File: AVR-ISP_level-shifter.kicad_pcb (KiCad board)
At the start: 2 copper layers, 0 parts

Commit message: Might be done!
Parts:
- added C1: 1µF, Resistors_SMD:R_0603, B.Cu at (63.2, 55.0)
- added C2: 1µF, Resistors_SMD:R_0603, B.Cu at (66.0, 53.2)
- added INPUT1: AVR-ISP-6, DIL-Headers:DIL-3, F.Cu at (50.0, 49.2)
- added INPUT2: AVR-ISP-10, DIL-Headers:DIL-5, F.Cu at (56.2, 49.2)
- added LOGO1: LED_smile_silkscreen_5mm, led-smile:LED_smile_silkscreen_5mm, B.Cu at (49.9, 56.1)
- added LOGO2: OSHW-logo_silkscreen_5mm, oshw-logo:OSHW-logo_silkscreen_5mm, B.Cu at (86.8, 56.1)
- added OUTPUT1: AVR-ISP-6, DIL-Headers:DIL-3, F.Cu at (86.5, 49.2)
- added OUTPUT2: AVR-ISP-10, DIL-Headers:DIL-5, F.Cu at (80.8, 49.2)
- added Q1: BSS138, Housings_SOT-23_SOT-143_TSOT-6:SOT-23, F.Cu at (63.0, 42.5)
- added Q2: BSS138, Housings_SOT-23_SOT-143_TSOT-6:SOT-23, F.Cu at (66.2, 42.5)
- added Q3: BSS138, Housings_SOT-23_SOT-143_TSOT-6:SOT-23, F.Cu at (63.0, 47.0)
- added Q4: BSS138, Housings_SOT-23_SOT-143_TSOT-6:SOT-23, F.Cu at (66.2, 47.0)
- added Q5: BSS138, Housings_SOT-23_SOT-143_TSOT-6:SOT-23, F.Cu at (63.0, 51.5)
- added Q6: BSS138, Housings_SOT-23_SOT-143_TSOT-6:SOT-23, F.Cu at (66.2, 51.5)
- added Q7: BSS138, Housings_SOT-23_SOT-143_TSOT-6:SOT-23, F.Cu at (63.0, 56.0)
- added Q8: BSS138, Housings_SOT-23_SOT-143_TSOT-6:SOT-23, F.Cu at (66.2, 56.0)
- added R1: 1K5, Resistors_SMD:R_0603, F.Cu at (60.5, 42.5)
- added R2: 1K5, Resistors_SMD:R_0603, F.Cu at (68.8, 42.5)
- added R3: 1K5, Resistors_SMD:R_0603, F.Cu at (60.5, 47.0)
- added R4: 1K5, Resistors_SMD:R_0603, F.Cu at (68.8, 47.0)
- added R5: 1K5, Resistors_SMD:R_0603, F.Cu at (60.5, 51.5)
- added R6: 1K5, Resistors_SMD:R_0603, F.Cu at (68.8, 51.5)
- added R7: 1K5, Resistors_SMD:R_0603, F.Cu at (60.5, 56.0)
- added R8: 1K5, Resistors_SMD:R_0603, F.Cu at (68.8, 56.0)
- added SW1: APEM 25439NH, Switches:switch_vert_SPDT_ON-OFF-ON_TH_APEM-25439NH, F.Cu at (73.8, 49.2)
- added U1: AMS1117-3.3, SMD_Packages:SOT-223, B.Cu at (64.8, 47.5)
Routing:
- net /GND: track 0.00 -> 113.4 mm
- net /VCC_PRG: track 0.00 -> 71.0 mm, vias 0 -> 4
- net /VCC_TARGET: track 0.00 -> 51.1 mm
- net /MISO_TARGET: track 0.00 -> 34.4 mm
- net /SCK_TARGET: track 0.00 -> 26.3 mm, vias 0 -> 2
- net /MOSI_TARGET: track 0.00 -> 25.8 mm, vias 0 -> 2
- net /RESET_TARGET: track 0.00 -> 24.4 mm, vias 0 -> 2
- net /MISO_PRG: track 0.00 -> 23.1 mm
- net /MOSI_PRG: track 0.00 -> 22.8 mm
- net /RESET_PRG: track 0.00 -> 20.8 mm
- net /VCC_REG: track 0.00 -> 16.4 mm
- net /SCK_PRG: track 0.00 -> 13.9 mm
- net Net-(Q7-Pad3): track 0.00 -> 1.25 mm
- net Net-(Q5-Pad3): track 0.00 -> 1.25 mm
- net Net-(Q3-Pad3): track 0.00 -> 1.25 mm
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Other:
- board outline added: 44 x 20 mm
- net class Default: trace_width 0.3048 -> 0.2032
- net class power added: clearance 0.2032, trace_width 0.4064, via_dia 0.635, via_drill 0.3302
- board text added: "2015 - blog.spitzenpfeil.org"
- board text added: "3.3V"
- board text added: "5V"
- board text added: "AVR-ISP"
- board text added: "AVR-ISP level-shifter 0.10.a"
- board text added: "INPUT"
- board text added: "OUTPUT"

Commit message: Tweaks.
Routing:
- net /MOSI_TARGET: track 25.8 -> 25.3 mm
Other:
- board text added: "[3.3-OFF-5]"

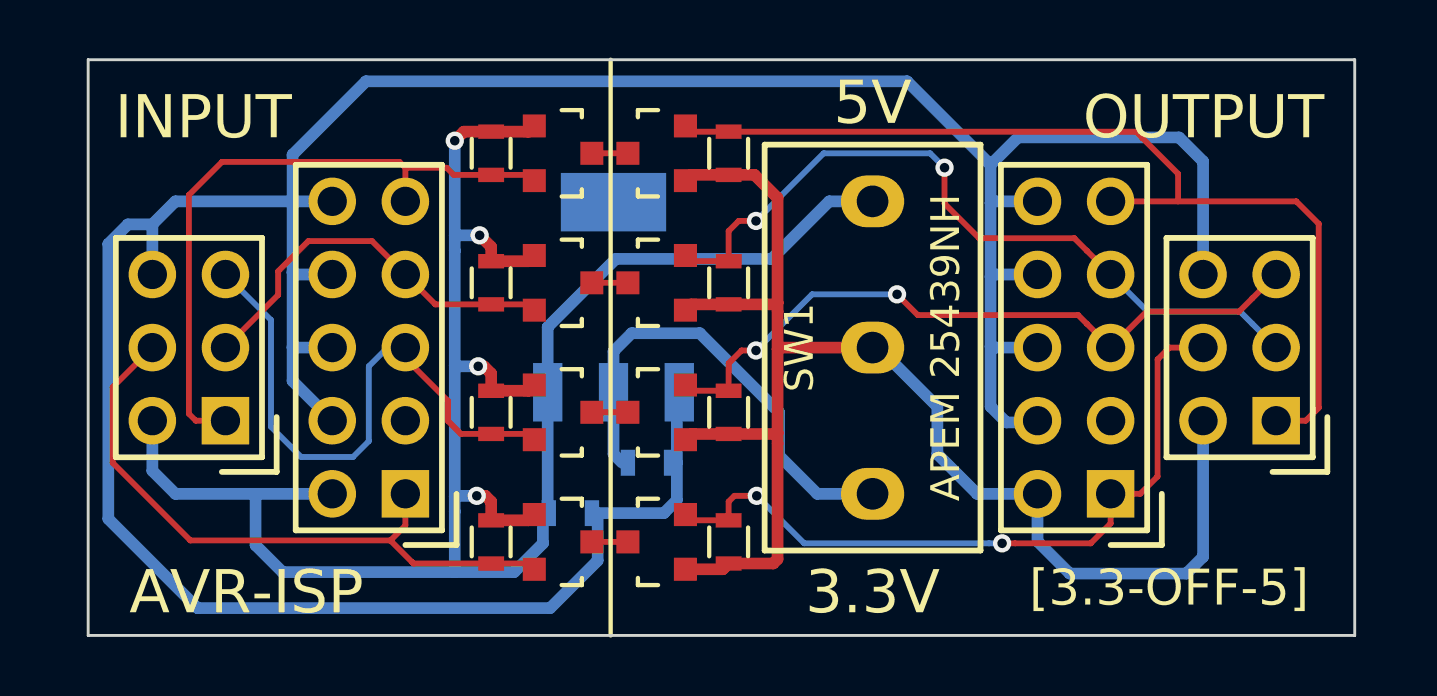
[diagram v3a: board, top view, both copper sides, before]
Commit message: Added shortened URL to github repo to board.
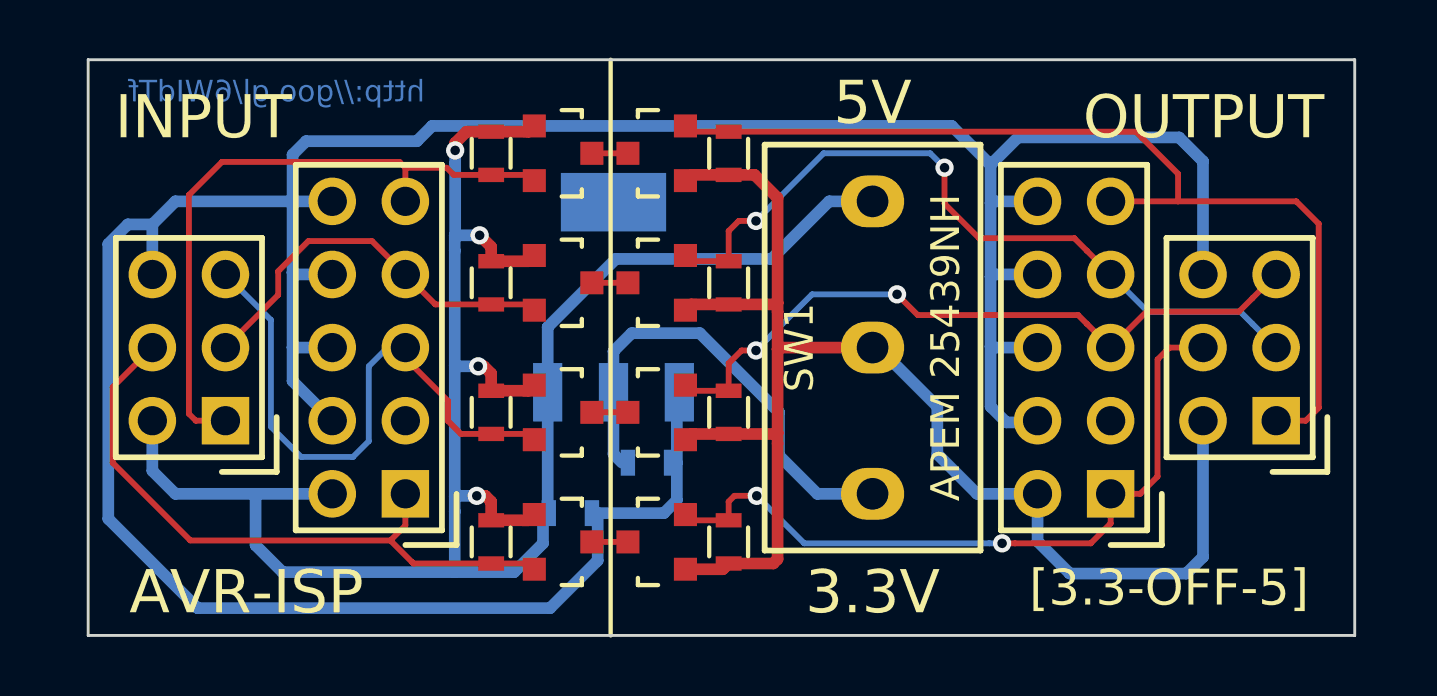
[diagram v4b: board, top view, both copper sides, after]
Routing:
- net /GND: track 113.4 -> 112.1 mm
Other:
- board text added: "http://goo.gl/6WIdTf"

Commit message: Added comment to schematic + silkscreen tweaks.
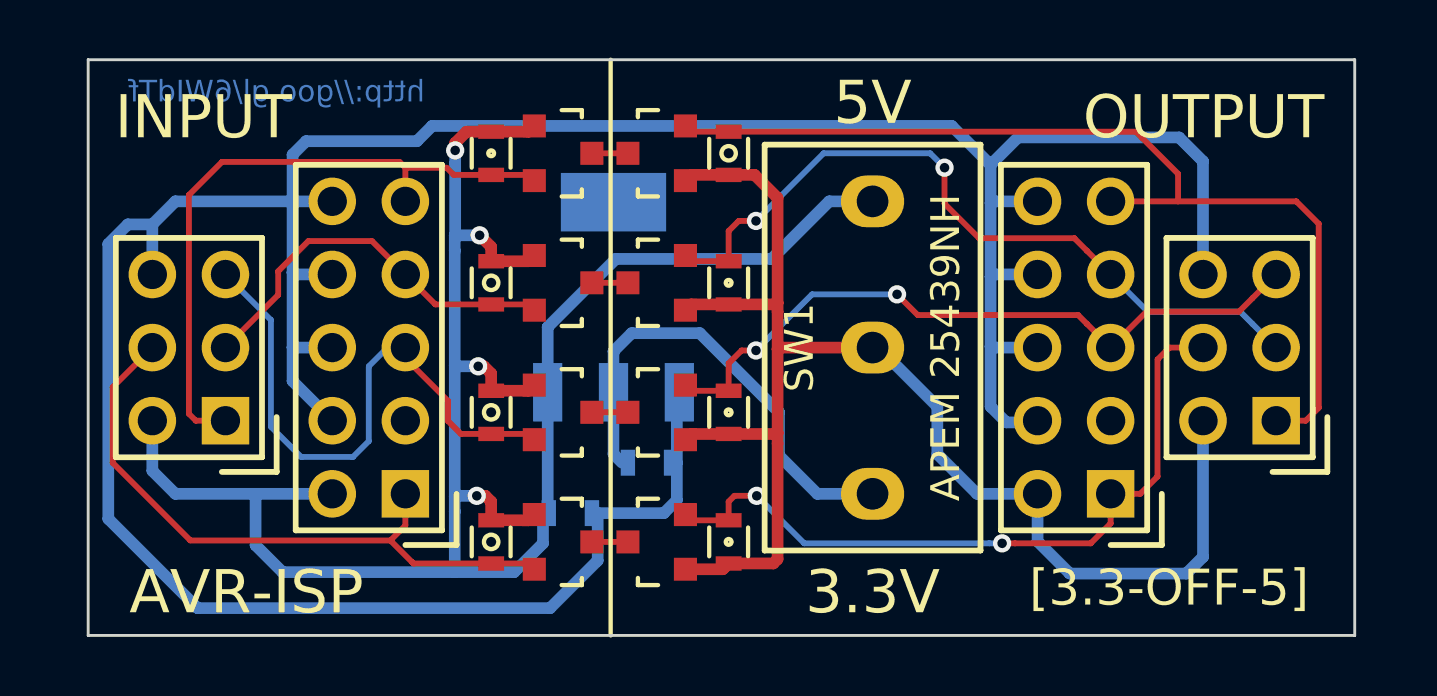
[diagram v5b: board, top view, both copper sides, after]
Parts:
- renumbered R2 to DR.R2, R3 to DR.R3, R5 to DR.R5, R7 to DR.R7
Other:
- board text added: "AVR-ISP level-shifter 0.11.a"
- board text removed: "AVR-ISP level-shifter 0.10.a"

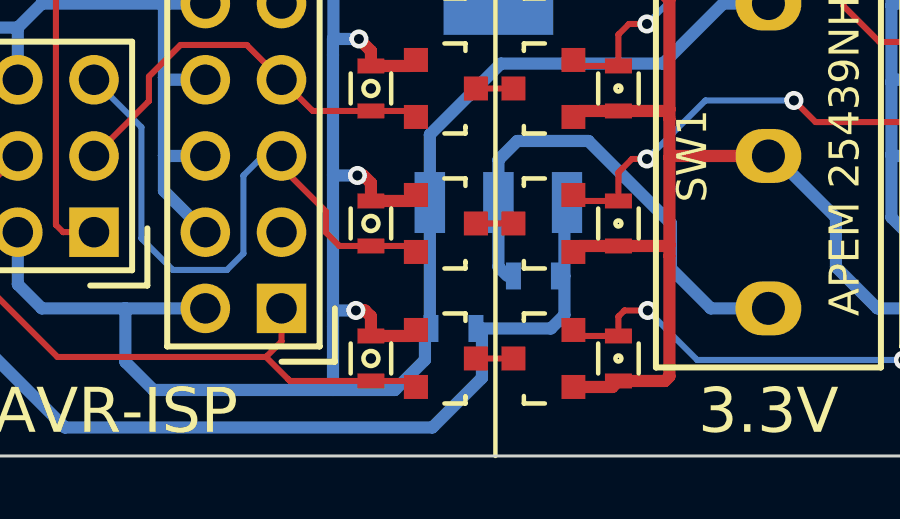
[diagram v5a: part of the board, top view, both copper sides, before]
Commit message: Added load resistor (~300R) to pull minimum load current out of 3.3V LDO.
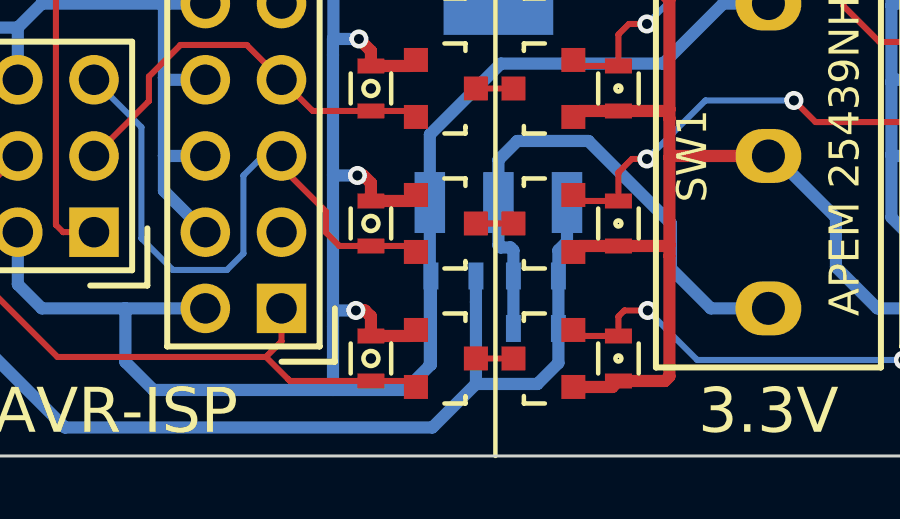
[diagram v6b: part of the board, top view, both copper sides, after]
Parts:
- added R9: 300R, Resistors_SMD:R_0603, B.Cu at (66.0, 55.0)
- moved C1 1.75 mm to (63.2, 53.2)
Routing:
- net /GND: track 112.1 -> 115.6 mm
- net /VCC_PRG: track 71.0 -> 74.2 mm
- net /VCC_REG: track 16.4 -> 18.5 mm
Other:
- board text added: "AVR-ISP level-shifter 0.12.a"
- board text removed: "AVR-ISP level-shifter 0.11.a"
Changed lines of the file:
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@@
 (kicad_pcb (version 4) (host pcbnew "(2015-04-23 BZR 5622)-product")
   (general
-    (links 64)
+    (links 66)
     (no_connects 0)
     (area 41.601086 39.174999 99.85 63.850001)
     (thickness 1.6)
     (drawings 24)
-    (tracks 272)
+    (tracks 279)
     (zones 0)
-    (modules 26)
+    (modules 27)
     (nets 17)
   )
@@
   (title_block
     (title AVR-ISP_level-shifter)
-    (date "Fri 24 Apr 2015")
-    (rev 0.11.a)
+    (date "Tue 05 May 2015")
+    (rev 0.12.a)
     (company "2015 - blog.spitzenpfeil.org")
   )
@@
   )
   (module Resistors_SMD:R_0603 (layer B.Cu)
-    (at 63.25 55)
+    (at 63.25 53.25)
     (descr "Resistor SMD 0603, reflow soldering, Vishay (see dcrcw.pdf)")
     (tags "resistor 0603")
@@
     )
   )
+  (module Resistors_SMD:R_0603 (layer B.Cu)
+    (at 66 55)
+    (descr "Resistor SMD 0603, reflow soldering, Vishay (see dcrcw.pdf)")
+    (tags "resistor 0603")
+    (attr smd)
+    (fp_text reference R9 (at 2.3 0) (layer B.SilkS)
+      (effects (font (size 1 1) (thickness 0.15)) (justify mirror))
+    )
+    (fp_text value 300R (at 0 -1.9) (layer B.Fab) hide
+      (effects (font (size 1 1) (thickness 0.15)) (justify mirror))
+    )
+    (fp_line (start -1.3 0.8) (end 1.3 0.8) (layer B.CrtYd) (width 0.05))
+    (fp_line (start -1.3 -0.8) (end 1.3 -0.8) (layer B.CrtYd) (width 0.05))
+    (fp_line (start -1.3 0.8) (end -1.3 -0.8) (layer B.CrtYd) (width 0.05))
+    (fp_line (start 1.3 0.8) (end 1.3 -0.8) (layer B.CrtYd) (width 0.05))
+    (fp_line (start 0.5 -0.675) (end -0.5 -0.675) (layer B.SilkS) (width 0.15))
+    (fp_line (start -0.5 0.675) (end 0.5 0.675) (layer B.SilkS) (width 0.15))
+    (pad 1 smd rect (at -0.75 0) (size 0.5 0.9) (layers B.Cu B.Mask)
+      (net 3 /VCC_REG))
+    (pad 2 smd rect (at 0.75 0) (size 0.5 0.9) (layers B.Cu B.Mask)
+      (net 2 /GND))
+    (model Resistors_SMD.3dshapes/R_0603.wrl
+      (at (xyz 0 0 0))
+      (scale (xyz 1 1 1))
+      (rotate (xyz 0 0 0))
+    )
+  )
   (gr_circle (center 68.75 56) (end 68.65 56) (layer F.SilkS) (width 0.15))
   (gr_circle (center 68.75 51.5) (end 68.85 51.5) (layer F.SilkS) (width 0.15))
@@
     (effects (font (size 1.25 1.25) (thickness 0.3)) (justify mirror))
   )
-  (gr_text "AVR-ISP level-shifter 0.11.a" (at 68.95 57.45) (layer B.SilkS)
+  (gr_text "AVR-ISP level-shifter 0.12.a" (at 68.95 57.45) (layer B.SilkS)
     (effects (font (size 1.2 1.2) (thickness 0.3)) (justify mirror))
   )
@@
   (segment (start 59.235737 45.884378) (end 59.235737 49.879509) (width 0.4064) (layer B.Cu) (net 1))
   (segment (start 53.25 57.05) (end 59.235737 57.05) (width 0.4064) (layer B.Cu) (net 1))
-  (segment (start 59.235737 57.05) (end 61.3 57.05) (width 0.4064) (layer B.Cu) (net 1))
   (segment (start 52.315443 54.33) (end 52.315443 56.115443) (width 0.4064) (layer B.Cu) (net 1))
   (segment (start 52.315443 56.115443) (end 53.25 57.05) (width 0.4064) (layer B.Cu) (net 1))
-  (segment (start 61.3 57.05) (end 62.3 56.05) (width 0.4064) (layer B.Cu) (net 1))
-  (segment (start 62.3 56.05) (end 62.3 55) (width 0.4064) (layer B.Cu) (net 1))
   (segment (start 52.315443 54.33) (end 49.53 54.33) (width 0.4064) (layer B.Cu) (net 1))
   (segment (start 54.98 54.33) (end 52.315443 54.33) (width 0.4064) (layer B.Cu) (net 1))
@@
   (segment (start 62.464 48.536) (end 64.83 46.17) (width 0.4064) (layer B.Cu) (net 1))
   (segment (start 62.464 50.802) (end 62.464 48.536) (width 0.4064) (layer B.Cu) (net 1))
-  (segment (start 62.464 50.802) (end 62.464 54.836) (width 0.4064) (layer B.Cu) (net 1))
-  (segment (start 62.464 54.836) (end 62.3 55) (width 0.4064) (layer B.Cu) (net 1))
   (segment (start 61.84924 50.4) (end 61.99924 50.55) (width 0.2032) (layer F.Cu) (net 1))
   (segment (start 61.84924 54.9) (end 61.99924 55.05) (width 0.2032) (layer F.Cu) (net 1))
@@
   (segment (start 59.6436 41.75) (end 59.25 42.1436) (width 0.4064) (layer F.Cu) (net 1))
   (segment (start 59.25 42.1436) (end 59.25 42.399998) (width 0.4064) (layer F.Cu) (net 1))
+  (segment (start 61.65 57.05) (end 62.5 56.2) (width 0.4064) (layer B.Cu) (net 1))
+  (segment (start 59.235737 57.05) (end 61.65 57.05) (width 0.4064) (layer B.Cu) (net 1))
+  (segment (start 62.5 56.2) (end 62.5 53.25) (width 0.4064) (layer B.Cu) (net 1))
+  (segment (start 62.464 56.164) (end 62.464 50.802) (width 0.4064) (layer B.Cu) (net 1))
+  (segment (start 62.5 56.2) (end 62.464 56.164) (width 0.4064) (layer B.Cu) (net 1))
   (segment (start 48.73 44.97) (end 47.88 44.97) (width 0.4064) (layer B.Cu) (net 2))
   (segment (start 47.88 44.97) (end 47.2 45.65) (width 0.4064) (layer B.Cu) (net 2))
@@
   (segment (start 47.2 55.2) (end 50.3 58.3) (width 0.4064) (layer B.Cu) (net 2))
   (segment (start 50.3 58.3) (end 62.55 58.3) (width 0.4064) (layer B.Cu) (net 2))
-  (segment (start 62.55 58.3) (end 64.2 56.65) (width 0.4064) (layer B.Cu) (net 2))
-  (segment (start 64.2 56.65) (end 64.2 55) (width 0.4064) (layer B.Cu) (net 2))
   (segment (start 53.6 46.638385) (end 53.6 44.170938) (width 0.4064) (layer B.Cu) (net 2))
   (segment (start 53.6 44.170938) (end 53.599062 44.17) (width 0.4064) (layer B.Cu) (net 2))
@@
   (segment (start 78.4 51.85) (end 79.42 51.85) (width 0.4064) (layer B.Cu) (net 2))
   (segment (start 79.42 51.85) (end 79.48 51.79) (width 0.4064) (layer B.Cu) (net 2))
-  (segment (start 66.5 55) (end 66.95 54.55) (width 0.4064) (layer B.Cu) (net 2))
-  (segment (start 66.95 54.55) (end 66.95 53.25) (width 0.4064) (layer B.Cu) (net 2))
-  (segment (start 64.2 55) (end 66.5 55) (width 0.4064) (layer B.Cu) (net 2))
-  (segment (start 66.95 53.25) (end 66.95 50.888) (width 0.4064) (layer B.Cu) (net 2))
-  (segment (start 66.95 50.888) (end 67.036 50.802) (width 0.4064) (layer B.Cu) (net 2))
   (segment (start 76.5 41.55) (end 77.85 42.9) (width 0.4064) (layer B.Cu) (net 2))
   (segment (start 57.9194 42.0806) (end 58.45 41.55) (width 0.4064) (layer B.Cu) (net 2))
@@
   (segment (start 53.6 44.169062) (end 53.6 42.55) (width 0.4064) (layer B.Cu) (net 2))
   (segment (start 53.599062 44.17) (end 53.6 44.169062) (width 0.4064) (layer B.Cu) (net 2))
+  (segment (start 66.75 53.25) (end 66.75 55) (width 0.4064) (layer B.Cu) (net 2))
+  (segment (start 62.55 58.3) (end 64 56.85) (width 0.4064) (layer B.Cu) (net 2))
+  (segment (start 67.036 52.1076) (end 67.036 50.802) (width 0.4064) (layer B.Cu) (net 2))
+  (segment (start 66.75 52.3936) (end 67.036 52.1076) (width 0.4064) (layer B.Cu) (net 2))
+  (segment (start 66.75 53.25) (end 66.75 52.3936) (width 0.4064) (layer B.Cu) (net 2))
+  (segment (start 64 56.85) (end 66.05 56.85) (width 0.4064) (layer B.Cu) (net 2))
+  (segment (start 66.75 56.15) (end 66.75 55) (width 0.4064) (layer B.Cu) (net 2))
+  (segment (start 66.05 56.85) (end 66.75 56.15) (width 0.4064) (layer B.Cu) (net 2))
+  (segment (start 64 54.1064) (end 64 56.85) (width 0.4064) (layer B.Cu) (net 2))
+  (segment (start 64 53.25) (end 64 54.1064) (width 0.4064) (layer B.Cu) (net 2))
   (segment (start 64.75 50.802) (end 64.75 49.3796) (width 0.4064) (layer B.Cu) (net 3))
   (segment (start 65.3796 48.75) (end 67.75 48.75) (width 0.4064) (layer B.Cu) (net 3))
@@
   (segment (start 70.5 53) (end 71.83 54.33) (width 0.4064) (layer B.Cu) (net 3))
   (segment (start 71.83 54.33) (end 73.75 54.33) (width 0.4064) (layer B.Cu) (net 3))
-  (segment (start 64.75 50.802) (end 64.75 52.95) (width 0.4064) (layer B.Cu) (net 3))
-  (segment (start 64.75 52.95) (end 65.05 53.25) (width 0.4064) (layer B.Cu) (net 3))
+  (segment (start 65.25 55) (end 65.25 53.25) (width 0.4064) (layer B.Cu) (net 3))
+  (segment (start 65.25 52.3936) (end 65.1564 52.3) (width 0.4064) (layer B.Cu) (net 3))
+  (segment (start 65.25 53.25) (end 65.25 52.3936) (width 0.4064) (layer B.Cu) (net 3))
+  (segment (start 64.75 52.2244) (end 64.75 50.802) (width 0.4064) (layer B.Cu) (net 3))
+  (segment (start 64.8256 52.3) (end 64.75 52.2244) (width 0.4064) (layer B.Cu) (net 3))
+  (segment (start 65.1564 52.3) (end 64.8256 52.3) (width 0.4064) (layer B.Cu) (net 3))
   (segment (start 58.952567 43.002567) (end 59.2 43.25) (width 0.2032) (layer F.Cu) (net 4))
   (segment (start 59.2 43.25) (end 60.5 43.25) (width 0.2032) (layer F.Cu) (net 4))
